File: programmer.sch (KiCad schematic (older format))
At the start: 59 parts, among them U15 93LCxxBT-I_OT, U16 FT2232H, U17 SN74LVC1G32DBVR, U18 SN74LVC2T45DCUR, U19 SN74LVC2T45DCUR, U20 SN74AXC4T245PWR, U21 SN74LVC2T45DCUR, U22 SN74LVC2T45DCUR, U23 SN74LVC2G07DCKR, U24 IS25LP080D, Y2 ECS-3225S33-120-FN-TR

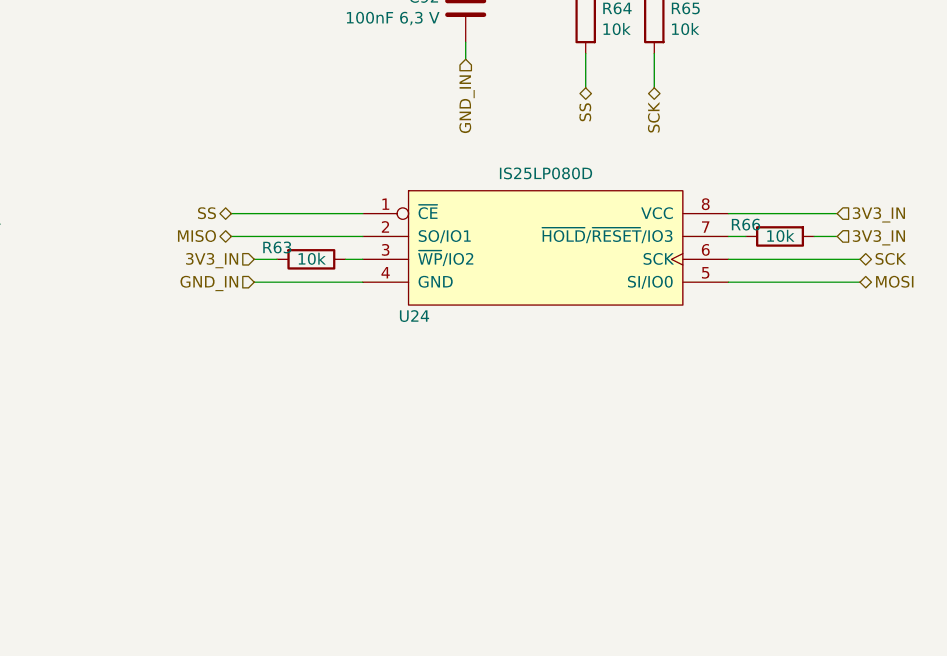
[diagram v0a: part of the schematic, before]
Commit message: 8MBit Flash swapped to a 64MBit one
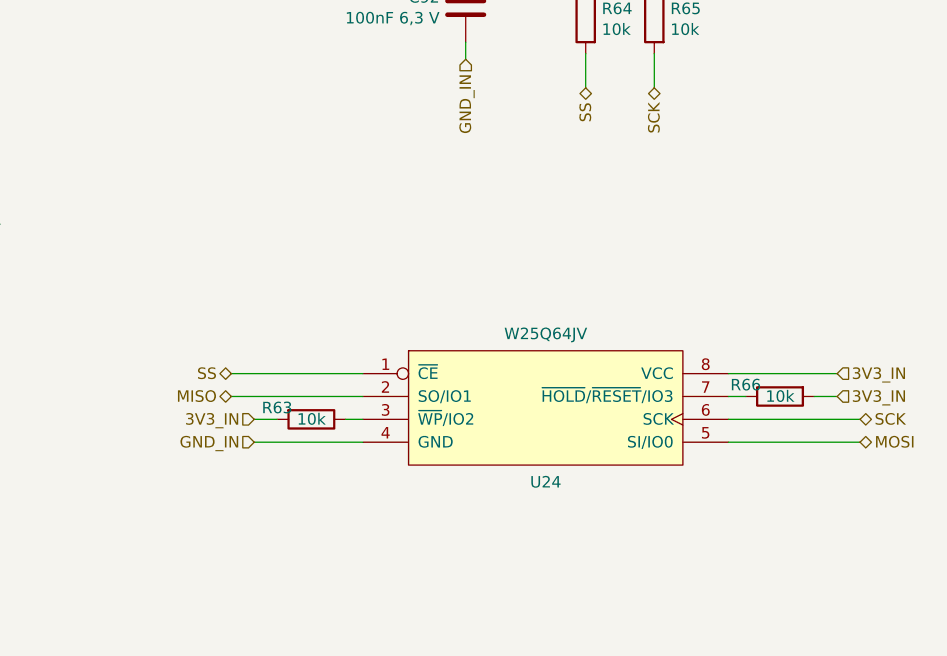
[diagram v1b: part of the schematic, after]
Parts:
- removed U24: IS25LP080D, Package_SO:SO-8_3.9x4.9mm_P1.27mm, symbol IS25LP080D:IS25LP080D
- added U24: W25Q64JV, Package_SO:SOIC-8_5.23x5.23mm_P1.27mm, symbol W25Q64JV:W25Q64JV
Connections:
- net 3V3_IN: now also U24.8 (VCC)
- net GND_IN: now also U24.4 (GND)
- net MISO: now also U24.2 (SO/IO1)
- net MOSI: now also U24.5 (SI/IO0)
- net SCK: now also U24.6 (SCK)
- net SS: now also U24.1 (~CE~)
- net at R63.1: now also U24.3 (~WP~/IO2)
- net at R66.1: now also U24.7 (~HOLD~/~RESET~/IO3)
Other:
- moved on the sheet: R63, R66
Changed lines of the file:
@@
 	-1   0    0    -1
 $EndComp
-$Comp
-L IS25LP080D:IS25LP080D U24
-U 1 1 5CAC0F76
-P 14075 8175
-F 0 "U24" H 13500 7875 50  0000 C CNN
-F 1 "IS25LP080D" H 14075 8499 50  0000 C CNN
-F 2 "Package_SO:SO-8_3.9x4.9mm_P1.27mm" H 14075 7775 50  0001 C CNN
-F 3 "http://www.issi.com/WW/pdf/25LP-WP080D.pdf" H 14075 7775 50  0001 C CNN
-F 4 "IC FLASH 8M SPI 133MHZ 8SOP" H 0   0   50  0001 C CNN "Description"
-F 5 "706-1580-ND" H 0   0   50  0001 C CNN "Digikey"
-F 6 "ISSI, Integrated Silicon Solution Inc" H 0   0   50  0001 C CNN "Mfg Name"
-F 7 "IS25LP080D-JNLE" H 0   0   50  0001 C CNN "Mfg Part Num"
-F 8 "Spec" H 0   0   50  0001 C CNN "Spec"
-	1    14075 8175
-	1    0    0    -1
-$EndComp
-Wire Wire Line
-	12700 8025 13275 8025
-Wire Wire Line
-	15450 8325 14875 8325
-Wire Wire Line
-	12700 8125 13275 8125
-Wire Wire Line
-	15450 8225 14875 8225
+Wire Wire Line
+	12700 8725 13275 8725
+Wire Wire Line
+	15450 9025 14875 9025
+Wire Wire Line
+	12700 8825 13275 8825
+Wire Wire Line
+	15450 8925 14875 8925
 Wire Wire Line
 	5025 4425 5025 4350
@@
 	3125 7625 3175 7625
 Wire Wire Line
-	15350 8025 14875 8025
-Wire Wire Line
-	12800 8325 13275 8325
+	15350 8725 14875 8725
+Wire Wire Line
+	12800 9025 13275 9025
 Wire Wire Line
 	4625 4425 4625 4350
@@
 L Device:R R66
 U 1 1 5CD40B26
-P 15100 8125
-F 0 "R66" V 15050 8275 50  0000 C CNN
-F 1 "10k" V 15100 8125 50  0000 C CNN
-F 2 "Resistor_SMD:R_0603_1608Metric" V 15030 8125 50  0001 C CNN
-F 3 "~" H 15100 8125 50  0001 C CNN
-F 4 "RES 10K OHM 5% 1/10W 0603" H 0   0   50  0001 C CNN "Description"
-F 5 "RMCF0603JT10K0CT-ND" H 0   0   50  0001 C CNN "Digikey"
-F 6 "Stackpole Electronics Inc" H 0   0   50  0001 C CNN "Mfg Name"
-F 7 "RMCF0603JT10K0" H 0   0   50  0001 C CNN "Mfg Part Num"
-F 8 "Any" H 0   0   50  0001 C CNN "Spec"
-	1    15100 8125
+P 15100 8825
+F 0 "R66" V 15050 8975 50  0000 C CNN
+F 1 "10k" V 15100 8825 50  0000 C CNN
+F 2 "Resistor_SMD:R_0603_1608Metric" V 15030 8825 50  0001 C CNN
+F 3 "~" H 15100 8825 50  0001 C CNN
+F 4 "RES 10K OHM 5% 1/10W 0603" H 0   700 50  0001 C CNN "Description"
+F 5 "RMCF0603JT10K0CT-ND" H 0   700 50  0001 C CNN "Digikey"
+F 6 "Stackpole Electronics Inc" H 0   700 50  0001 C CNN "Mfg Name"
+F 7 "RMCF0603JT10K0" H 0   700 50  0001 C CNN "Mfg Part Num"
+F 8 "Any" H 0   700 50  0001 C CNN "Spec"
+	1    15100 8825
 	0    -1   1    0
 $EndComp
 Wire Wire Line
-	14875 8125 14950 8125
-Wire Wire Line
-	15350 8125 15250 8125
+	14875 8825 14950 8825
+Wire Wire Line
+	15350 8825 15250 8825
 $Comp
 L Device:R R63
 U 1 1 5CD829A8
-P 13050 8225
-F 0 "R63" V 13000 8075 50  0000 C CNN
-F 1 "10k" V 13050 8225 50  0000 C CNN
-F 2 "Resistor_SMD:R_0603_1608Metric" V 12980 8225 50  0001 C CNN
-F 3 "~" H 13050 8225 50  0001 C CNN
-F 4 "RES 10K OHM 5% 1/10W 0603" H 0   0   50  0001 C CNN "Description"
-F 5 "RMCF0603JT10K0CT-ND" H 0   0   50  0001 C CNN "Digikey"
-F 6 "Stackpole Electronics Inc" H 0   0   50  0001 C CNN "Mfg Name"
-F 7 "RMCF0603JT10K0" H 0   0   50  0001 C CNN "Mfg Part Num"
-F 8 "Any" H 0   0   50  0001 C CNN "Spec"
-	1    13050 8225
+P 13050 8925
+F 0 "R63" V 13000 8775 50  0000 C CNN
+F 1 "10k" V 13050 8925 50  0000 C CNN
+F 2 "Resistor_SMD:R_0603_1608Metric" V 12980 8925 50  0001 C CNN
+F 3 "~" H 13050 8925 50  0001 C CNN
+F 4 "RES 10K OHM 5% 1/10W 0603" H 0   700 50  0001 C CNN "Description"
+F 5 "RMCF0603JT10K0CT-ND" H 0   700 50  0001 C CNN "Digikey"
+F 6 "Stackpole Electronics Inc" H 0   700 50  0001 C CNN "Mfg Name"
+F 7 "RMCF0603JT10K0" H 0   700 50  0001 C CNN "Mfg Part Num"
+F 8 "Any" H 0   700 50  0001 C CNN "Spec"
+	1    13050 8925
 	0    1    1    0
 $EndComp
 Wire Wire Line
-	13275 8225 13200 8225
-Wire Wire Line
-	12800 8225 12900 8225
+	13275 8925 13200 8925
+Wire Wire Line
+	12800 8925 12900 8925
 $Comp
 L Device:R R64
@@
 Text HLabel 14400 6975 1    50   Input ~ 0
 3V3_IN
-Text HLabel 15350 8025 2    50   Input ~ 0
+Text HLabel 15350 8725 2    50   Input ~ 0
 3V3_IN
-Text HLabel 15350 8125 2    50   Input ~ 0
+Text HLabel 15350 8825 2    50   Input ~ 0
 3V3_IN
-Text HLabel 12800 8225 0    50   Input ~ 0
+Text HLabel 12800 8925 0    50   Input ~ 0
 3V3_IN
-Text HLabel 12800 8325 0    50   Input ~ 0
+Text HLabel 12800 9025 0    50   Input ~ 0
 GND_IN
 Text HLabel 13725 7350 3    50   Input ~ 0
@@
 Text HLabel 11375 8600 2    50   Input ~ 0
 ~DSR~
-Text HLabel 12700 8025 0    50   BiDi ~ 0
+Text HLabel 12700 8725 0    50   BiDi ~ 0
 SS
-Text HLabel 12700 8125 0    50   BiDi ~ 0
+Text HLabel 12700 8825 0    50   BiDi ~ 0
 MISO
-Text HLabel 15450 8225 2    50   BiDi ~ 0
+Text HLabel 15450 8925 2    50   BiDi ~ 0
 SCK
-Text HLabel 15450 8325 2    50   BiDi ~ 0
+Text HLabel 15450 9025 2    50   BiDi ~ 0
 MOSI
 Text HLabel 14250 7475 3    50   BiDi ~ 0
@@
 	7175 10150 6475 10150
 Connection ~ 6475 10150
+$Comp
+L W25Q64JV:W25Q64JV U24
+U 1 1 5EED1082
+P 14075 8875
+F 0 "U24" H 14075 8550 50  0000 C CNN
+F 1 "W25Q64JV" H 14075 9199 50  0000 C CNN
+F 2 "Package_SO:SOIC-8_5.23x5.23mm_P1.27mm" H 14075 8475 50  0001 C CNN
+F 3 "https://www.winbond.com/resource-files/w25q64jv%20revj%2003272018%20plus.pdf" H 14075 8475 50  0001 C CNN
+F 4 "IC FLASH 64M SPI 133MHZ 8SOIC" H 14075 8875 50  0001 C CNN "Description"
+F 5 "W25Q64JVSSIMCT-ND" H 14075 8875 50  0001 C CNN "Digikey"
+F 6 "Winbond Electronics" H 14075 8875 50  0001 C CNN "Mfg Name"
+F 7 "W25Q64JVSSIM TR" H 14075 8875 50  0001 C CNN "Mfg Part Num"
+F 8 "Spec" H 14075 8875 50  0001 C CNN "Spec"
+	1    14075 8875
+	1    0    0    -1
+$EndComp
 $EndSCHEMATC
